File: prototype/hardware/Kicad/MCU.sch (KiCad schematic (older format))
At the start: 31 parts, among them J1 Conn_01x05, J5 Conn_01x04, U11 W25Q64JVSSIM, U7 ATSAMD21J18A-AU, Y3 16MHz

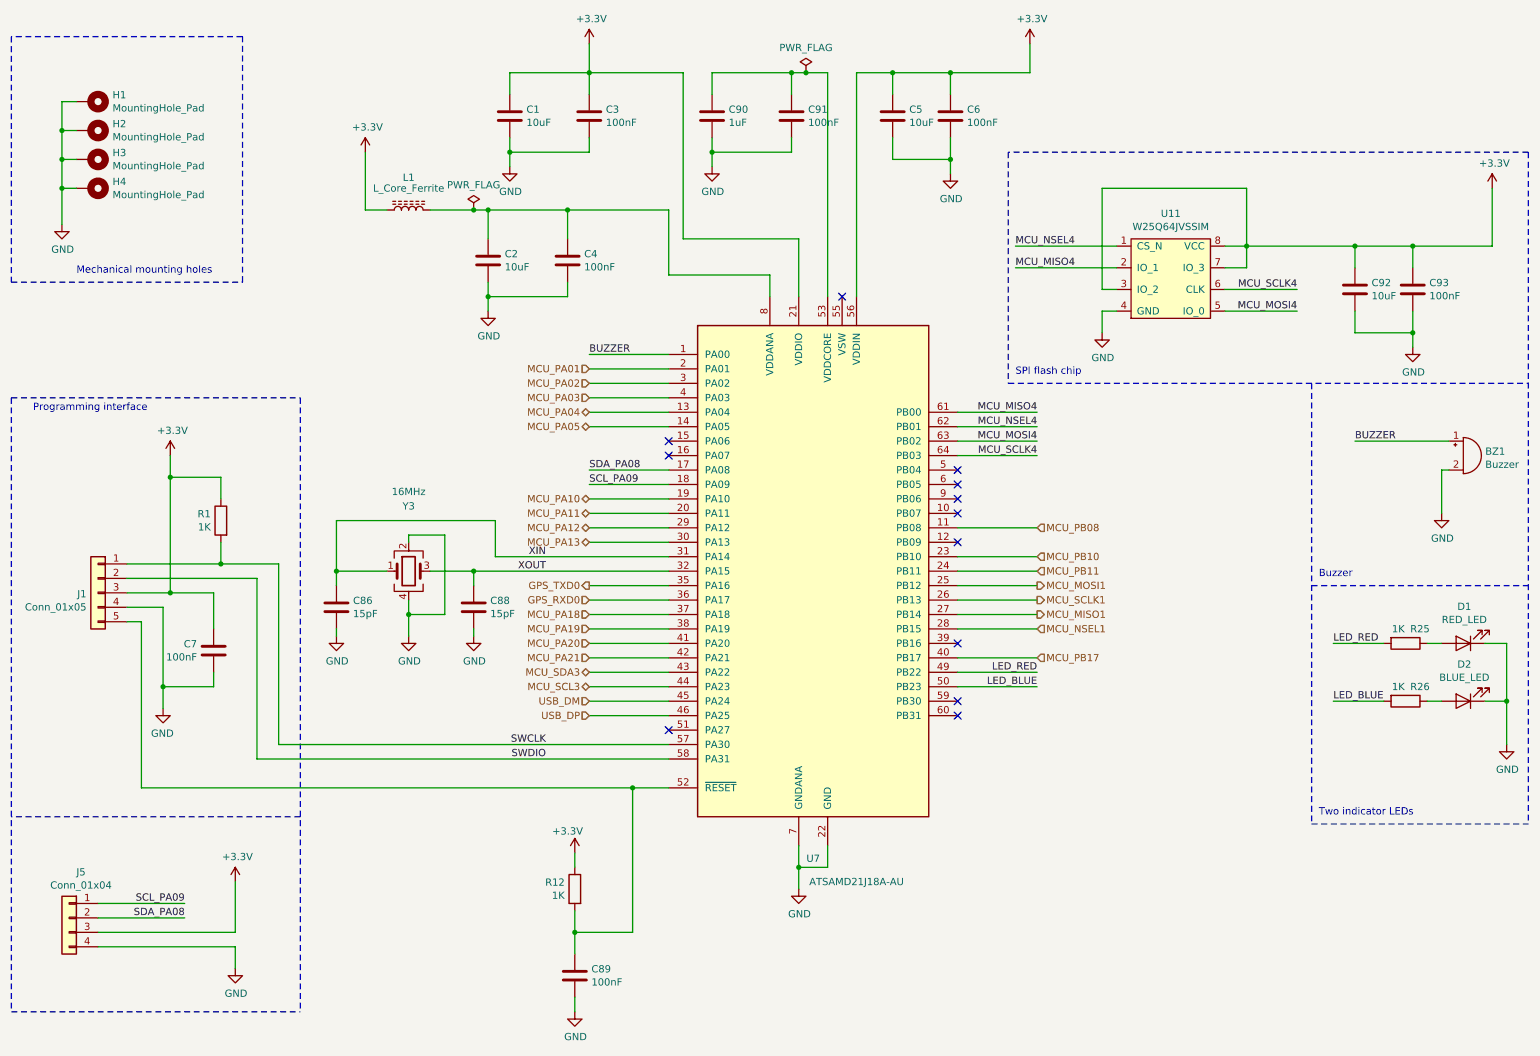
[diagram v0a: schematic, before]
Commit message: removed the samd21 and put in the murata
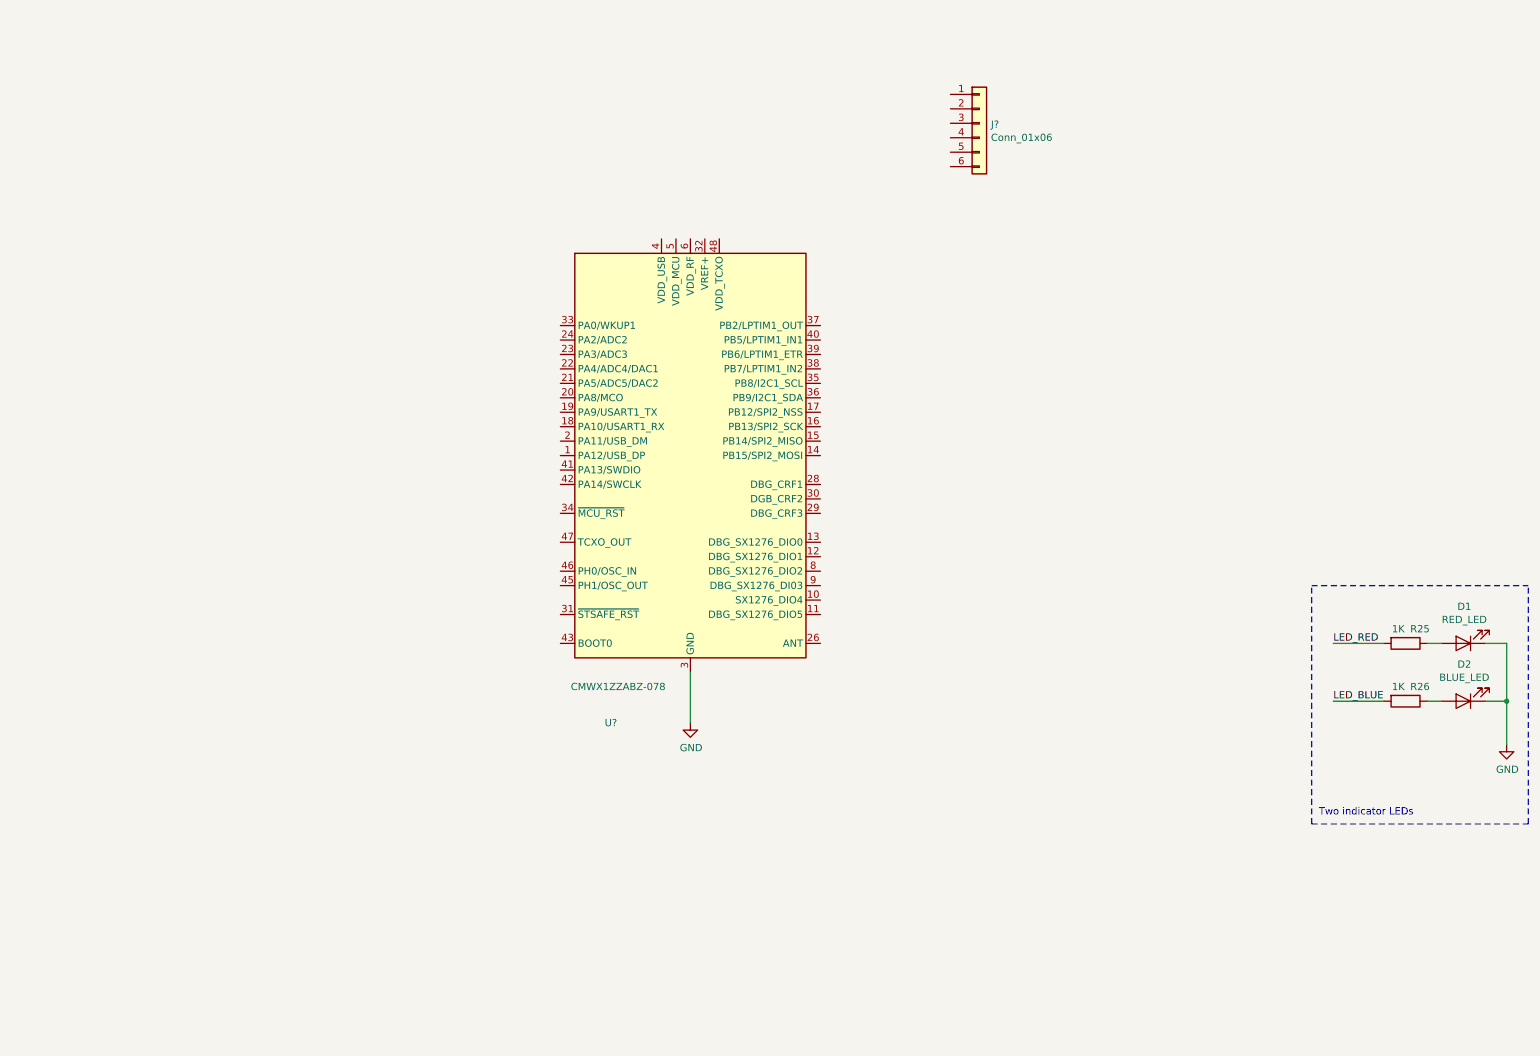
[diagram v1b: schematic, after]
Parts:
- removed BZ1: Buzzer, Buzzer_Beeper:Buzzer_12x9.5RM7.6, symbol Device:Buzzer
- removed C1, C2, C5, C92: 10uF, Capacitor_SMD:C_0603_1608Metric, symbol Device:C
- removed C3, C4, C6, C7, C89, C91, C93: 100nF, Capacitor_SMD:C_0603_1608Metric, symbol Device:C
- removed C86, C88: 15pF, Capacitor_SMD:C_0603_1608Metric, symbol Device:C
- removed C90: 1uF, Capacitor_SMD:C_0603_1608Metric, symbol Device:C
- removed H1, H2, H3, H4: MountingHole_Pad, MountingHole:MountingHole_3.2mm_M3_Pad, symbol Mechanical:MountingHole_Pad
- removed J1: Conn_01x05, Connector_PinHeader_2.54mm:PinHeader_1x05_P2.54mm_Vertical, symbol Connector_Generic:Conn_01x05
- removed J5: Conn_01x04, flight-computer:NS-Tech_Grove_1x04_P2mm_Vertical, symbol Connector_Generic:Conn_01x04
- removed L1: L_Core_Ferrite, Inductor_SMD:L_0603_1608Metric, symbol Device:L_Core_Ferrite
- removed R1, R12: 1K, Resistor_SMD:R_0603_1608Metric, symbol Device:R
- removed U11: W25Q64JVSSIM, Package_SO:SOIC-8_5.23x5.23mm_P1.27mm, symbol flight-computer:W25Q64JVSSIM
- removed U7: ATSAMD21J18A-AU, Package_QFP:TQFP-64_10x10mm_P0.5mm, symbol flight-computer:ATSAMD21J18A-AU
- removed Y3: 16MHz, flight-computer:Crystal_SMD_2520-4Pin_2.5x2.0mm, symbol Device:Crystal_GND24
- added J?: Conn_01x06, symbol Connector_Generic:Conn_01x06
- added U?: CMWX1ZZABZ-078, RF_Module:CMWX1ZZABZ, symbol RF_Module:CMWX1ZZABZ-078
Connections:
- net GND: now also U?.25 (GND), U?.27 (GND), U?.3 (GND), U?.44 (GND), U?.49 (GND), U?.50 (GND), U?.51 (GND), U?.52 (GND), U?.53 (GND), U?.54 (GND), U?.55 (GND), U?.56 (GND), U?.57 (GND), U?.7 (GND)
- no-connect marks 12 -> 0
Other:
- note removed: "Buzzer\n"
- note removed: "Mechanical mounting holes"
- note removed: "Programming interface\n"
- note removed: "SPI flash chip"

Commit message: programming interface done
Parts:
- added C?: 0.1uF 0402, symbol Device:C_Small
- added J?: Conn_Coaxial, symbol Connector:Conn_Coaxial
- added R?: 10K 0402, symbol Device:R
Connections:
- net GND: now also J?.3 (Pin_3), C?.2, J?.2 (Ext), R?.2
- net at U?.26 (ANT): now also J?.1 (In)
- net RESET: now reaches U?.34 (~MCU_RST)
- net RESET: now also J?.5 (Pin_5), C?.1
- net SWDIO: now reaches U?.41 (PA13/SWDIO)
- net SWDIO: now also J?.4 (Pin_4)
- net SWCLK: now reaches U?.42 (PA14/SWCLK)
- net SWCLK: now also J?.2 (Pin_2)
- net at U?.43 (BOOT0): now also R?.1
- net +3V3: now reaches J?.1 (Pin_1)
- no-connect marks 0 -> 1
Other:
- note added: "Debugging and programming\ninterface"
- moved on the sheet: J?
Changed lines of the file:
@@
 U 1 1 5DB27A2E
 P 5250 3600
-F 0 "U?" H 4700 1750 50  0000 C CNN
-F 1 "CMWX1ZZABZ-078" H 4750 2000 50  0000 C CNN
+F 0 "U?" H 4550 5200 50  0000 C CNN
+F 1 "CMWX1ZZABZ-078" H 4550 5050 50  0000 C CNN
 F 2 "RF_Module:CMWX1ZZABZ" H 5250 3600 50  0001 C CNN
 F 3 "https://wireless.murata.com/RFM/data/type_abz.pdf" H 7700 2100 50  0001 C CNN
 	1    5250 3600
-	1    0    0    -1
-$EndComp
-$Comp
-L Connector_Generic:Conn_01x06 J?
-U 1 1 5DB45FE9
-P 7250 1300
-F 0 "J?" H 7330 1292 50  0000 L CNN
-F 1 "Conn_01x06" H 7330 1201 50  0000 L CNN
-F 2 "" H 7250 1300 50  0001 C CNN
-F 3 "~" H 7250 1300 50  0001 C CNN
-	1    7250 1300
 	1    0    0    -1
 $EndComp
@@
 Wire Wire Line
 	5250 5450 5250 5100
+Wire Wire Line
+	6150 4900 7550 4900
+$Comp
+L Connector:Conn_Coaxial J?
+U 1 1 5DB4CA28
+P 7750 4900
+F 0 "J?" H 7850 4875 50  0000 L CNN
+F 1 "Conn_Coaxial" H 7850 4784 50  0000 L CNN
+F 2 "" H 7750 4900 50  0001 C CNN
+F 3 " ~" H 7750 4900 50  0001 C CNN
+	1    7750 4900
+	1    0    0    -1
+$EndComp
+$Comp
+L power:GND #PWR?
+U 1 1 5DB4D709
+P 7750 5400
+F 0 "#PWR?" H 7750 5150 50  0001 C CNN
+F 1 "GND" H 7755 5227 50  0000 C CNN
+F 2 "" H 7750 5400 50  0001 C CNN
+F 3 "" H 7750 5400 50  0001 C CNN
+	1    7750 5400
+	1    0    0    -1
+$EndComp
+Wire Wire Line
+	7750 5400 7750 5100
+Wire Wire Line
+	4350 4900 4000 4900
+Wire Wire Line
+	4000 4900 4000 5000
+$Comp
+L power:GND #PWR?
+U 1 1 5DB50FAC
+P 4000 5450
+F 0 "#PWR?" H 4000 5200 50  0001 C CNN
+F 1 "GND" H 4005 5277 50  0000 C CNN
+F 2 "" H 4000 5450 50  0001 C CNN
+F 3 "" H 4000 5450 50  0001 C CNN
+	1    4000 5450
+	1    0    0    -1
+$EndComp
+$Comp
+L Device:R R?
+U 1 1 5DB51493
+P 4000 5150
+F 0 "R?" H 4070 5196 50  0000 L CNN
+F 1 "10K 0402" H 4070 5105 50  0000 L CNN
+F 2 "" V 3930 5150 50  0001 C CNN
+F 3 "~" H 4000 5150 50  0001 C CNN
+	1    4000 5150
+	1    0    0    -1
+$EndComp
+Wire Wire Line
+	4000 5300 4000 5450
+Wire Wire Line
+	1950 3350 2350 3350
+Wire Wire Line
+	2350 3350 2350 3050
+$Comp
+L power:+3.3V #PWR?
+U 1 1 5DB55728
+P 2350 3050
+F 0 "#PWR?" H 2350 2900 50  0001 C CNN
+F 1 "+3.3V" H 2365 3223 50  0000 C CNN
+F 2 "" H 2350 3050 50  0001 C CNN
+F 3 "" H 2350 3050 50  0001 C CNN
+	1    2350 3050
+	-1   0    0    -1
+$EndComp
+$Comp
+L Connector_Generic:Conn_01x06 J?
+U 1 1 5DB45FE9
+P 1750 3550
+F 0 "J?" H 1668 3967 50  0000 C CNN
+F 1 "Conn_01x06" H 1668 3876 50  0000 C CNN
+F 2 "" H 1750 3550 50  0001 C CNN
+F 3 "~" H 1750 3550 50  0001 C CNN
+	1    1750 3550
+	-1   0    0    -1
+$EndComp
+Wire Wire Line
+	4350 3700 3950 3700
+Text Label 3950 3700 0    50   ~ 0
+SWDIO
+Wire Wire Line
+	1950 3450 2250 3450
+Wire Wire Line
+	1950 3550 2350 3550
+Wire Wire Line
+	2350 3550 2350 4050
+Wire Wire Line
+	1950 3650 2250 3650
+NoConn ~ 1950 3850
+Text Label 3950 3800 0    50   ~ 0
+SWCLK
+Wire Wire Line
+	3950 3800 4350 3800
+Text Label 2250 3450 2    50   ~ 0
+SWCLK
+Text Label 2250 3650 2    50   ~ 0
+SWDIO
+$Comp
+L power:GND #PWR?
+U 1 1 5DB70B69
+P 2350 4050
+F 0 "#PWR?" H 2350 3800 50  0001 C CNN
+F 1 "GND" H 2355 3877 50  0000 C CNN
+F 2 "" H 2350 4050 50  0001 C CNN
+F 3 "" H 2350 4050 50  0001 C CNN
+	1    2350 4050
+	1    0    0    -1
+$EndComp
+Wire Notes Line
+	750  2400 750  4750
+Wire Notes Line
+	750  4750 2700 4750
+Wire Notes Line
+	2700 4750 2700 2350
+Wire Notes Line
+	2700 2350 750  2350
+Text Notes 900  4600 0    50   ~ 0
+Debugging and programming\ninterface
+Wire Wire Line
+	1950 3750 2250 3750
+Text Label 2250 3750 2    50   ~ 0
+RESET
+Wire Wire Line
+	4350 4000 3550 4000
+Text Label 3250 4000 0    50   ~ 0
+RESET
+Wire Wire Line
+	3550 4000 3550 4250
+Connection ~ 3550 4000
+Wire Wire Line
+	3550 4000 3250 4000
+$Comp
+L power:GND #PWR?
+U 1 1 5DB7C91C
+P 3550 4600
+F 0 "#PWR?" H 3550 4350 50  0001 C CNN
+F 1 "GND" H 3555 4427 50  0000 C CNN
+F 2 "" H 3550 4600 50  0001 C CNN
+F 3 "" H 3550 4600 50  0001 C CNN
+	1    3550 4600
+	1    0    0    -1
+$EndComp
+$Comp
+L Device:C_Small C?
+U 1 1 5DB7CD5A
+P 3550 4350
+F 0 "C?" H 3642 4396 50  0000 L CNN
+F 1 "0.1uF 0402" H 3642 4305 50  0000 L CNN
+F 2 "" H 3550 4350 50  0001 C CNN
+F 3 "~" H 3550 4350 50  0001 C CNN
+	1    3550 4350
+	1    0    0    -1
+$EndComp
+Wire Wire Line
+	3550 4450 3550 4600
 $EndSCHEMATC
